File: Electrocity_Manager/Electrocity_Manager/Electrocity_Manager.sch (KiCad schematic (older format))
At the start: 193 parts, among them IC2 MAIN_SHUTDOWN, IC3 RELAY_STATE, IC4 ADC_RST, J1 SERIAL, P1 SWD, P10 EMERGENCY, P11 EMERGENCY, P12 FRAME_GRAND, P13 BATT_IN, P14 POWER_OUT, P15 FUN_OUT, P16 BATT_IN, P17 POWER_OUT, P18 FUN_OUT, P2 CAN, P3 CAN, P4 EMERGENCY_SIGNAL, P5 EMERGENCY_SIGNAL, P6 12V_OUT, P7 12V_OUT, P9 MAIN_SW, Q1 FET_N, Q2 NPN, Q3 NPN, Q4 NPN, Q5 NPN, Q6 NPN, Q7 FET_N, SW1 RST, U1 MAX3051, U10 BD9G101G, U11 ACS781, U12 V23134J1052D642, U13 ACS70331, U14 ACS781, U15 BD33FA1, U16 EC12PLRGBSDVBF, U17 LOGO, U18 LOGO, U19 MCP2221A, U2 STM32F405RG, U20 OSRB38C9AA, U21 OSRB38C9AA, U22 HSIN_946, U3 FULLCOLOR, U4 AQM0802_BL, U5 AP3211, U6 SI8900, U7 AZ1086H, U8 V23134J1052D642, U9 RPA60-12FW/P, X1 8MHz

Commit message: 電源配線完了.フルカラーの秋月のエンコーダ基板面積的に使用できなかった...
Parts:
- removed C45: 0.1u, Mizz_lib:C_0603, symbol device:C
- removed Q4, Q5, Q6: NPN, Mizz_lib:SOT-123, symbol device:NPN
- removed R49: 510, Mizz_lib:R_0603, symbol device:R
- removed R50, R54, R55: 10k, Mizz_lib:R_0603, symbol device:R
- removed R56, R57: 100, Mizz_lib:R_0603, symbol device:R
- removed U16: EC12PLRGBSDVBF, Mizz_lib:EC12PLRGBSDVBF, symbol Miz:EC12PLRGBSDVBF
- removed U3: FULLCOLOR, Mizz_lib:OSTBABS4C2B, symbol myDevice:OSTBABS4C2B
- added C49: 10u, Mizz_lib:C_0603, symbol device:C
- added SW2: SW0, Mizz_lib:SW_SPST_CK_RS282G05A3, symbol device:SW_PUSH
- added SW3: SW1, Mizz_lib:SW_SPST_CK_RS282G05A3, symbol device:SW_PUSH
- added U16: LOGO, Mizz_lib:Robocon2019_30.0x30.0_silk, symbol Electrocity_Manager-rescue:LOGO-myDevice
- added U23: LOGO, Mizz_lib:Battery_Killer_logo, symbol Electrocity_Manager-rescue:LOGO-myDevice
- added U3: FULL COLOR, Mizz_lib:OSTBABS4C2B, symbol Electrocity_Manager-rescue:OSTBABS4C2B-myDevice
- C24, C26: value 22u -> 10u
- D1, D11, D12, D13, D21, D22, D23, D24, D25, D29, D9: symbol device:DIODE -> Electrocity_Manager-rescue:DIODE-device
- J1: symbol Connector:USB_B_Micro -> Electrocity_Manager-rescue:USB_B_Micro-Connector
- Q1, Q7: symbol Hori_lib:MOSFET_N_123 -> Electrocity_Manager-rescue:MOSFET_N_123-Hori_lib
- Q2, Q3: symbol device:NPN -> Electrocity_Manager-rescue:NPN-device
- R1, R5: value 510 -> 330
- R22, R23: value 330 -> 10k
- U1: footprint Package_TO_SOT_SMD:SOT-23-8 -> Mizz_lib:SOIC-8_3.9x4.9mm_Pitch1.27mm; symbol myDevice:MAX3051 -> Electrocity_Manager-rescue:MAX3051-myDevice
- U10: symbol myDevice:BD9G101G -> Electrocity_Manager-rescue:BD9G101G-myDevice
- U17, U18: symbol myDevice:LOGO -> Electrocity_Manager-rescue:LOGO-myDevice
- U2: footprint Housings_QFP:TQFP-64_10x10mm_Pitch0.5mm -> Package_QFP:LQFP-64_10x10mm_P0.5mm
- U4: symbol Hori_lib:AQM0802_BL -> Electrocity_Manager-rescue:AQM0802_BL-Hori_lib
- U6: symbol Hori_lib:SI8900 -> Electrocity_Manager-rescue:SI8900-Hori_lib
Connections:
- net +12C: now also C30.2; no longer C30.1, IC3.1
- net +3.3V: now also R22.1, R23.1, C49.1
- net ADC12_IN1: now also C33.1, R40.1; no longer C44.1, R52.1, R53.2
- net ADC12_IN4: no longer C33.1, R40.1
- net ADC12_IN5: no longer C39.1, R44.1
- net ADC12_IN6: no longer C42.1, R47.1
- net Coil: now also IC3.1
- net GND: now also Q2.2 (E), Q3.2 (E), C49.2, SW2.1, SW3.1, U3.4 (red_K), U3.5 (green_K), U3.6 (blue_K); no longer R1.1, R24.1, R29.1, R5.1
- net PB0: no longer U2.26 (ADC12_IN8/TIM1_CH2N/TIM8_CH2N/TIM3_CH3/PB0)
- net PB1: no longer U2.27 (ADC12_IN9/TIM1_CH3N/TIM8_CH3N/TIM3_CH4/PB1)
- net PB12: no longer R10.1
- net PB13: no longer R13.1
- net PB14: no longer R14.1
- net PB15: now also IC4.1; no longer R16.1
- net PB2: no longer IC4.1
- net PC15: no longer R48.1
- net PC2: now also R18.2, R48.1
- net PC4: now also R23.2, SW3.2
- net PC5: now also R22.2, SW2.2
- net TIM1_CH2: now also R21.1; no longer R23.1
- net TIM1_CH3: now also R5.1; no longer R22.1
- net TIM1_CH4: now also R1.1; no longer R21.1
- net TIM8_CH1: no longer U2.37 (PC6/TIM8_CH1/USART6_TX/TIM3_CH1)
- net ADC12_IN2: now reaches U2.14 (UART4_TX/TIM2_CH1_ETR/ADC12_IN0/TIM5_CH1/PA0)
- net ADC12_IN2: now also C39.1, R44.1
- net PC7: now reaches U2.38 (PC7/TIM8_CH2/USART6_RX/TIM3_CH2)
- net PC7: now also R13.1
- net PC8: now reaches U2.39 (PC8/TIM8_CH3/TIM3_CH3)
- net PC8: now also R14.1
- net PC9: now reaches U2.40 (PC9/TIM8_CH4/TIM3_CH4)
- net PC9: now also R16.1
- net at D9.1 (A), SP1.2: now also R24.2; no longer Q2.3 (C)
- net at R29.2: now also U4.11 (Cathode); no longer Q3.2 (E)
- net at Q3.3 (C): now also R29.1; no longer U4.11 (Cathode)
- net at R5.2: now also U3.2 (green_A)
- net at R1.2: now also U3.1 (blue_A)
- net at Q7.1 (G), R48.2: no longer R18.2
- net at R21.2: now also U3.3 (red_A)
- net at R41.2, R42.2, U10.3 (FB): now also C30.1; no longer C30.2
- new net: Q2.3 (C), R24.1
- new net ADC12_IN8: C44.1, R52.1, R53.2, U2.26 (ADC12_IN8/TIM1_CH2N/TIM8_CH2N/TIM3_CH3/PB0)
- new net ADC12_IN9: C42.1, R47.1, U2.27 (ADC12_IN9/TIM1_CH3N/TIM8_CH3N/TIM3_CH4/PB1)
- new net PC6: R10.1, U2.37 (PC6/TIM8_CH1/USART6_TX/TIM3_CH1)
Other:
- moved on the sheet: C30, Q2, Q3, R18, R20, R24, R28, R29, R41, R42, R48

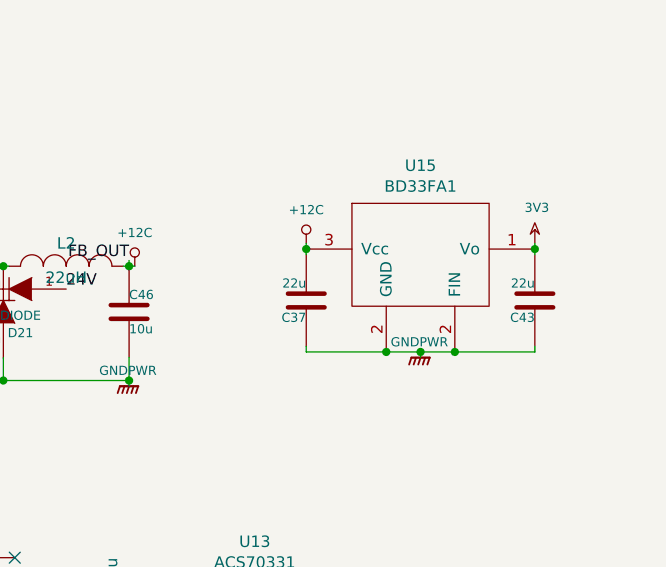
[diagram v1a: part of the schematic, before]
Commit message: mainは加工データを追加,電源はビアホールなどの配線の改良.
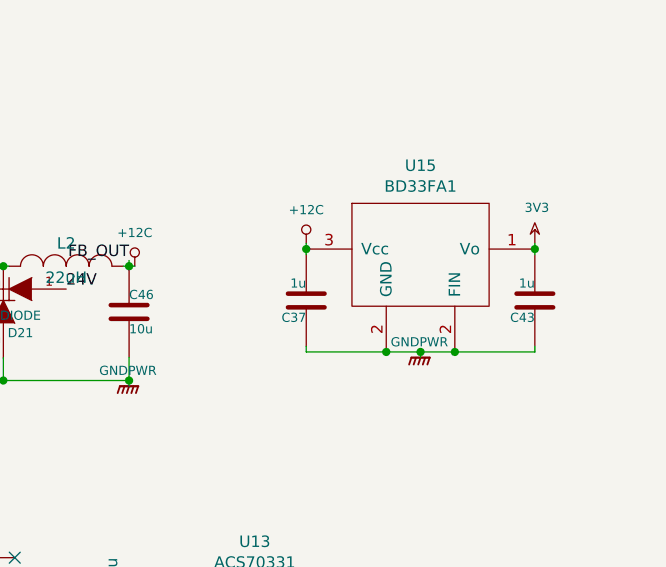
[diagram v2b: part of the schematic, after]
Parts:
- C37, C43: value 22u -> 1u
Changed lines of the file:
@@
 P 14550 6600
 F 0 "C37" H 14550 6675 40  0000 L CNN
-F 1 "22u" H 14550 6525 40  0000 L CNN
+F 1 "1u" H 14550 6525 40  0000 L CNN
 F 2 "Mizz_lib:C_0805" H 14588 6450 30  0001 C CNN
 F 3 "" H 14550 6600 60  0000 C CNN
@@
 P 15550 6600
 F 0 "C43" H 15550 6675 40  0000 L CNN
-F 1 "22u" H 15550 6525 40  0000 L CNN
+F 1 "1u" H 15550 6525 40  0000 L CNN
 F 2 "Mizz_lib:C_0603" H 15588 6450 30  0001 C CNN
 F 3 "" H 15550 6600 60  0000 C CNN
